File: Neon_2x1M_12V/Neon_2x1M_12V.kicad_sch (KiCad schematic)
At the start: 48 parts, among them J1 Conn_01x16_Pin, J2 Barrel_Jack_MountingPin, J3 Conn_01x16_Pin, J4 Barrel_Jack_MountingPin, J5 Barrel_Jack_MountingPin, J6 Conn_01x03_Pin, Q1 IRLML2502TRPBF, Q2 IRLML2502TRPBF, Q3 Si2302DS, Q4 Si2302DS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

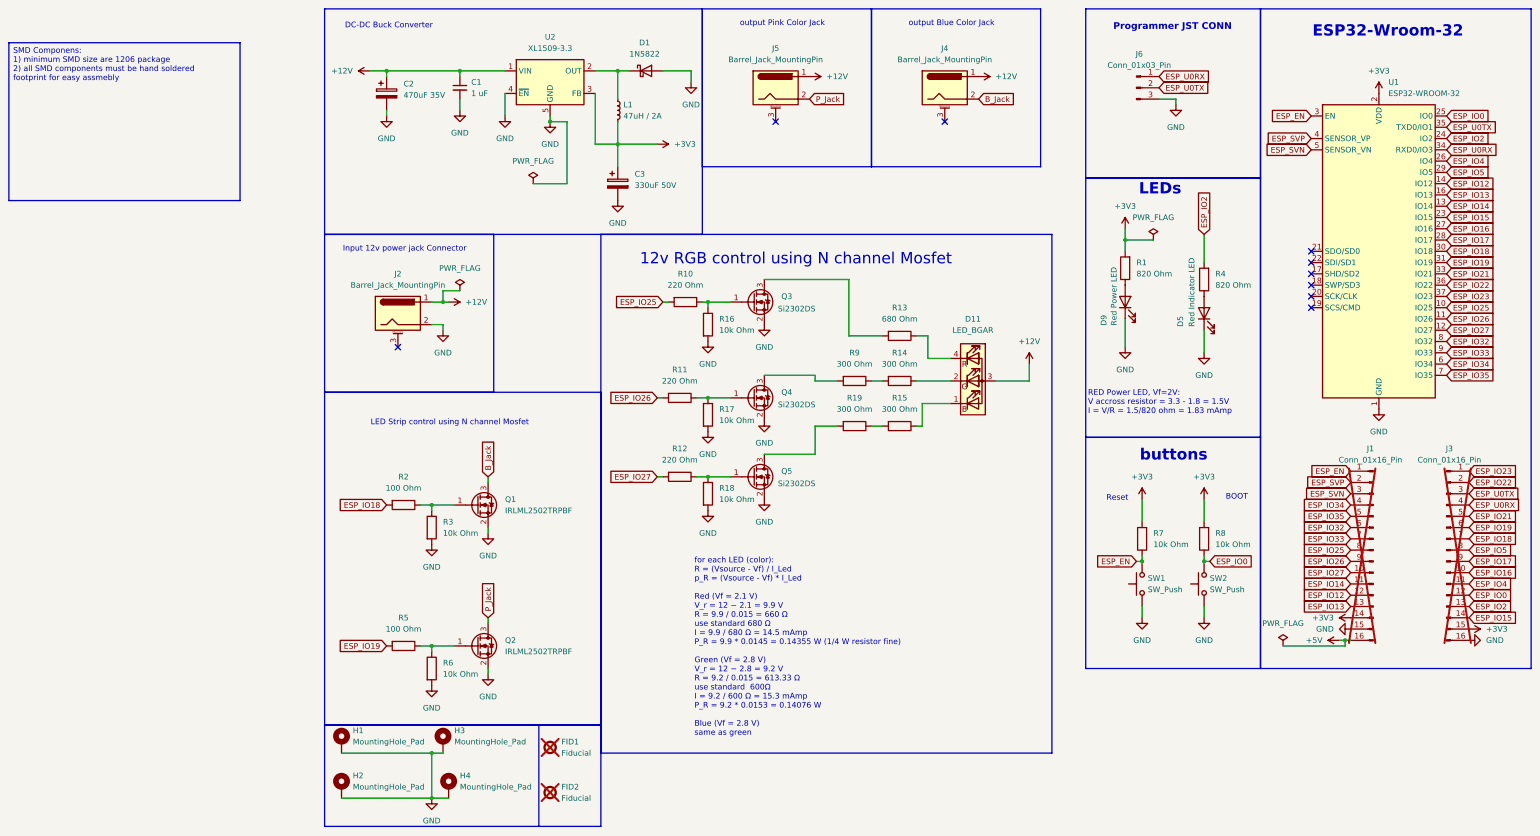
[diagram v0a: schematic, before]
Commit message: initial commit remove old chinese buck converter and replace it with LM2596 DC DC converter adjustable
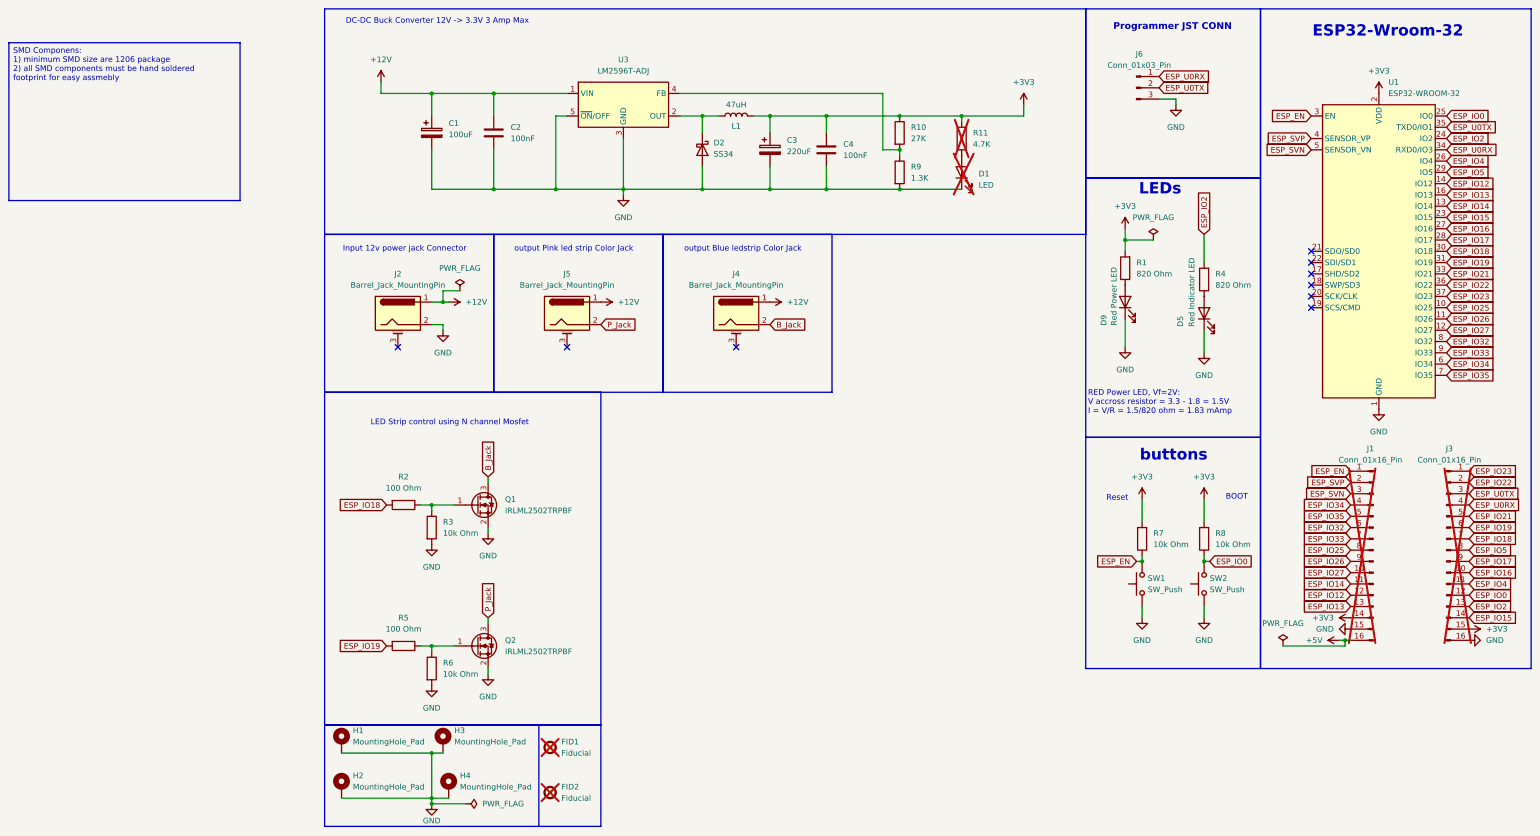
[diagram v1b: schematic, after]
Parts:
- removed C1: 1 uF, Capacitor_SMD:C_1206_3216Metric, symbol Device:C_Small
- removed C2: 470uF 35V, Capacitor_THT:CP_Radial_D10.0mm_P5.00mm, symbol Device:C_Polarized
- removed D1: 1N5822, Diode_SMD:D_SMA, symbol Device:D_Schottky
- removed D11: LED_BGAR, LED_THT:LED_D5.0mm-4_RGB, symbol Device:LED_BGAR
- removed L1: 47uH / 2A, CD43_Inductor:CD43, symbol Device:L_Small
- removed Q3: Si2302DS, custom_SOT23:custom_SOT23, symbol Transistor_FET:BSS138
- removed Q4, Q5: Si2302DS, Package_TO_SOT_SMD:SOT-23, symbol Transistor_FET:BSS138
- removed R12: 220 Ohm, Resistor_SMD:R_1206_3216Metric_Pad1.30x1.75mm_HandSolder, symbol Device:R
- removed R13: 680 Ohm, Resistor_SMD:R_1206_3216Metric_Pad1.30x1.75mm_HandSolder, symbol Device:R
- removed R14, R15, R19: 300 Ohm, Resistor_SMD:R_1206_3216Metric_Pad1.30x1.75mm_HandSolder, symbol Device:R
- removed R16, R17, R18: 10k Ohm, Resistor_SMD:R_0805_2012Metric_Pad1.20x1.40mm_HandSolder, symbol Device:R
- removed U2: XL1509-3.3, Package_SO:SOIC-8_3.9x4.9mm_P1.27mm, symbol Regulator_Switching:XL1509-3.3
- added C1: 100uF, Capacitor_SMD:C_Elec_8x10.2, symbol Device:C_Polarized
- added C2, C4: 100nF, Capacitor_SMD:C_1206_3216Metric_Pad1.33x1.80mm_HandSolder, symbol Device:C
- added D1: LED, symbol Device:LED
- added D2: SS34, Diode_SMD:D_SMA_Handsoldering, symbol Diode:SS34
- added L1: 47uH, Inductor_SMD:L_Bourns_SRR1208_12.7x12.7mm, symbol Device:L
- added U3: LM2596T-ADJ, Package_TO_SOT_THT:TO-220-5_P3.4x3.7mm_StaggerOdd_Lead3.8mm_Vertical, symbol Regulator_Switching:LM2596T-ADJ
- C3: value 330uF 50V -> 220uF; footprint Capacitor_SMD:CP_Elec_10x10.5 -> Capacitor_SMD:C_Elec_8x10.2; link https://uge-one.com/product/smd-aluminum-electrolytic-capac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 -> (none)
- R10: value 220 Ohm -> 27K; link https://uge-one.com/product/smd-chip-resistor-size-1206-220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 -> (none)
- R11: value 220 Ohm -> 4.7K; footprint Resistor_SMD:R_1206_3216Metric_Pad1.30x1.75mm_HandSolder -> (none); link https://uge-one.com/product/smd-chip-resistor-size-1206-220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 -> (none); now not fitted; now left out of the parts list
- R9: value 300 Ohm -> 1.3K; link https://uge-one.com/product/smd-chip-resistor-size-1206-300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 -> (none)
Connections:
- net +12V: now also C1.1, C2.1, U3.1 (VIN)
- net +3V3: now also R10.1, R11.1, C4.1, L1.2
- net ESP_IO25: no longer R10.2
- net ESP_IO26: no longer R11.2
- net GND: now also R9.2, C1.2, C2.2, C4.2, D1.1 (K), D2.2 (A), U3.3 (GND), U3.5 (~{ON}/OFF)
- net at R9.1: now also R10.2, U3.4 (FB)
- new net: D2.1 (K), L1.1, U3.2 (OUT)
- new net: D1.2 (A), R11.2
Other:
- note added: "DC-DC Buck Converter 12V -> 3.3V 3 Amp Max"
- note added: "output Blue ledstrip Color Jack"
- note added: "output Pink led strip Color Jack"
- note removed: "12v RGB control using N channel Mosfet"
- note removed: "DC-DC Buck Converter"
- note removed: "for each LED (color): R = (Vsource - Vf) / I_Led p_R = (Vsource - Vf) * I_Led Red (Vf = 2.1 V) V_r = 12 − 2.1 = 9.9 V R = 9.9 / 0.015 = 660 Ω use standard 680 Ω I = 9.9 / 680 Ω = 14.5 mAmp P_R = 9.9 * 0.0145 = 0.14355 W (1/4 W resistor fine) Green (Vf = 2.8 V) V_r = 12 − 2.8 = 9.2 V R = 9.2 / 0.015 = 613.33 Ω use standard 600Ω I = 9.2 / 600 Ω = 15.3 mAmp P_R = 9.2 * 0.0153 = 0.14076 W Blue (Vf = 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"
- note removed: "output Blue Color Jack"
- note removed: "output Pink Color Jack"
- title: Neon 1meter 12V -> Neon 1meter 12V V2.0
- moved on the sheet: J4, J5
